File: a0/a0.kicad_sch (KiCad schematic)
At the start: 0 parts

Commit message: update A0
Signed-off-by: Rodney Osodo <socials@rodneyosodo.com>
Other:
- company: (none) -> Abstract Machines
- title: (none) -> A0
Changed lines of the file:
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@@
 	(generator_version "9.0")
 	(paper "A4")
+	(title_block
+		(title "A0")
+		(date "2026-07-03")
+		(rev "v0.4.0")
+		(company "Abstract Machines")
+		(comment 1 "Designed By: Osodo Rodney")
+		(comment 2 "Approved By: Jones Kisaka")
+		(comment 3 "Approved By: Jeff Mboya")
+	)
 	(sheet
 		(at 128.27 78.74)
@@
 		(on_board yes)
 		(dnp no)
-		(fields_autoplaced yes)
 		(stroke
 			(width 0.1524)
@@
 		)
 		(fill
-			(color 0 0 0 0.0000)
+			(color 255 0 0 0.3000)
 		)
 		(property "Sheetname" "power"
-			(at 128.27 78.0284 0)
+			(at 152.654 107.696 0)
 			(effects
 				(font
-					(size 1.27 1.27)
+					(size 7.9756 7.9756)
+					(thickness 1.5951)
+					(bold yes)
 				)
 				(justify left bottom)
@@
 		(on_board yes)
 		(dnp no)
-		(fields_autoplaced yes)
 		(stroke
 			(width 0.1524)
@@
 		)
 		(fill
-			(color 0 0 0 0.0000)
+			(color 255 229 191 1.0000)
 		)
 		(property "Sheetname" "ESP32-C6"
-			(at 31.75 25.9584 0)
+			(at 36.068 50.8 0)
 			(effects
 				(font
-					(size 1.27 1.27)
+					(size 7.9756 7.9756)
+					(thickness 1.5951)
+					(bold yes)
 				)
 				(justify left bottom)
@@
 		(on_board yes)
 		(dnp no)
-		(fields_autoplaced yes)
 		(stroke
 			(width 0.1524)
@@
 		)
 		(fill
-			(color 0 0 0 0.0000)
+			(color 255 255 194 1.0000)
 		)
 		(property "Sheetname" "sim7080G"
-			(at 127 24.6884 0)
+			(at 134.62 50.292 0)
 			(effects
 				(font
-					(size 1.27 1.27)
+					(size 7.9756 7.9756)
+					(thickness 1.5951)
+					(bold yes)
 				)
 				(justify left bottom)
@@
 		(on_board yes)
 		(dnp no)
-		(fields_autoplaced yes)
 		(stroke
 			(width 0.1524)
@@
 		)
 		(fill
-			(color 0 0 0 0.0000)
+			(color 0 0 255 0.3000)
 		)
 		(property "Sheetname" "wmbus"
-			(at 33.02 80.5684 0)
+			(at 47.752 109.474 0)
 			(effects
 				(font
-					(size 1.27 1.27)
+					(size 7.9756 7.9756)
+					(thickness 1.5951)
+					(bold yes)
 				)
 				(justify left bottom)

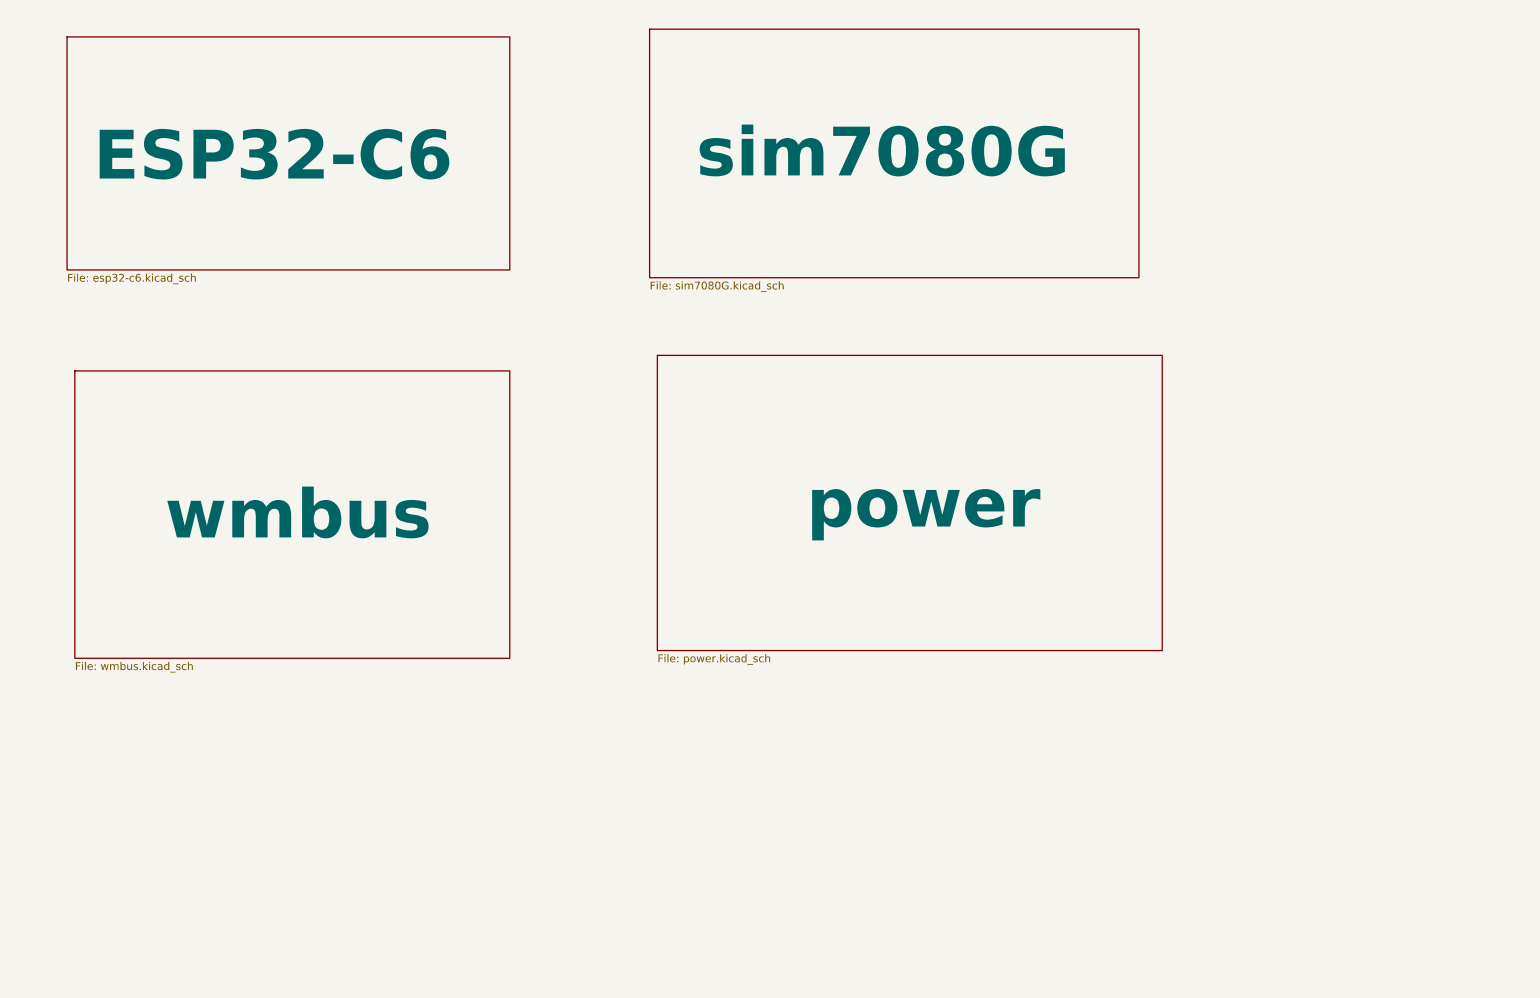
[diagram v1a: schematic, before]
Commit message: fix(A0): update to use modules
Signed-off-by: Rodney Osodo <socials@rodneyosodo.com>
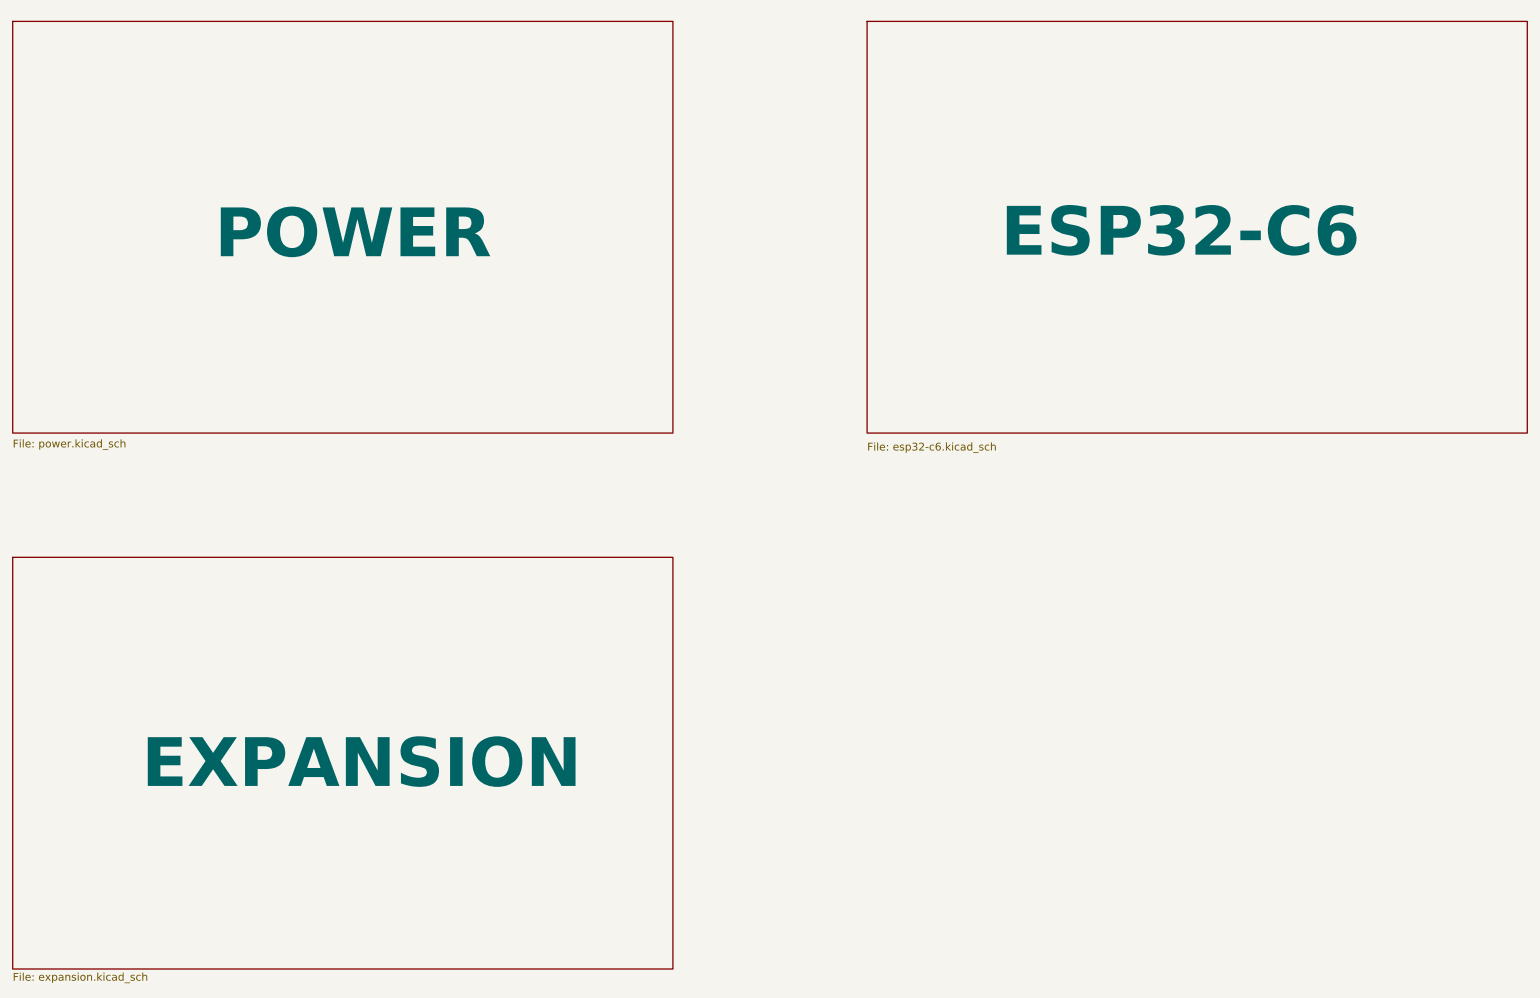
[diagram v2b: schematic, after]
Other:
- sheet power renamed POWER
- removed sheet sim7080G
- removed sheet wmbus
- added sheet EXPANSION (expansion.kicad_sch)
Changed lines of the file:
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@@
 	(title_block
 		(title "A0")
-		(date "2026-07-03")
-		(rev "v0.4.0")
+		(date "2026-07-09")
+		(rev "v0.5.0")
 		(company "Abstract Machines")
 		(comment 1 "Designed By: Osodo Rodney")
@@
 	)
 	(sheet
-		(at 128.27 78.74)
-		(size 82.55 48.26)
+		(at 22.86 24.13)
+		(size 107.95 67.31)
 		(exclude_from_sim no)
 		(in_bom yes)
@@
 			(color 255 0 0 0.3000)
 		)
-		(property "Sheetname" "power"
-			(at 152.654 107.696 0)
+		(property "Sheetname" "POWER"
+			(at 55.88 63.5 0)
 			(effects
 				(font
@@
 		)
 		(property "Sheetfile" "power.kicad_sch"
-			(at 128.27 127.5846 0)
+			(at 22.86 92.456 0)
 			(effects
 				(font
@@
 	)
 	(sheet
-		(at 31.75 26.67)
-		(size 72.39 38.1)
+		(at 22.86 111.76)
+		(size 107.95 67.31)
+		(exclude_from_sim no)
+		(in_bom yes)
+		(on_board yes)
+		(dnp no)
+		(stroke
+			(width 0.1524)
+			(type solid)
+		)
+		(fill
+			(color 132 0 132 0.5000)
+		)
+		(property "Sheetname" "EXPANSION"
+			(at 43.942 150.114 0)
+			(effects
+				(font
+					(size 7.9756 7.9756)
+					(thickness 1.5951)
+					(bold yes)
+				)
+				(justify left bottom)
+			)
+		)
+		(property "Sheetfile" "expansion.kicad_sch"
+			(at 22.86 179.6546 0)
+			(effects
+				(font
+					(size 1.27 1.27)
+				)
+				(justify left top)
+			)
+		)
+		(instances
+			(project "a0"
+				(path "/0ceabfe0-439b-45ca-b804-d1d856d0c97d"
+					(page "4")
+				)
+			)
+		)
+	)
+	(sheet
+		(at 162.56 24.13)
+		(size 107.95 67.31)
 		(exclude_from_sim no)
 		(in_bom yes)
@@
 		)
 		(property "Sheetname" "ESP32-C6"
-			(at 36.068 50.8 0)
+			(at 184.404 63.246 0)
 			(effects
 				(font
@@
 		)
 		(property "Sheetfile" "esp32-c6.kicad_sch"
-			(at 31.75 65.3546 0)
+			(at 162.56 92.964 0)
 			(effects
 				(font
@@
 				)
 			)
-		)
-	)
-	(sheet
-		(at 127 25.4)
-		(size 80.01 40.64)
-		(exclude_from_sim no)
-		(in_bom yes)
-		(on_board yes)
-		(dnp no)
-		(stroke
-			(width 0.1524)
-			(type solid)
-		)
-		(fill
-			(color 255 255 194 1.0000)
-		)
-		(property "Sheetname" "sim7080G"
-			(at 134.62 50.292 0)
-			(effects
-				(font
-					(size 7.9756 7.9756)
-					(thickness 1.5951)
-					(bold yes)
-				)
-				(justify left bottom)
-			)
-		)
-		(property "Sheetfile" "sim7080G.kicad_sch"
-			(at 127 66.6246 0)
-			(effects
-				(font
-					(size 1.27 1.27)
-				)
-				(justify left top)
-			)
-		)
-		(instances
-			(project "a0"
-				(path "/0ceabfe0-439b-45ca-b804-d1d856d0c97d"
-					(page "3")
-				)
-			)
-		)
-	)
-	(sheet
-		(at 33.02 81.28)
-		(size 71.12 46.99)
-		(exclude_from_sim no)
-		(in_bom yes)
-		(on_board yes)
-		(dnp no)
-		(stroke
-			(width 0.1524)
-			(type solid)
-		)
-		(fill
-			(color 0 0 255 0.3000)
-		)
-		(property "Sheetname" "wmbus"
-			(at 47.752 109.474 0)
-			(effects
-				(font
-					(size 7.9756 7.9756)
-					(thickness 1.5951)
-					(bold yes)
-				)
-				(justify left bottom)
-			)
-		)
-		(property "Sheetfile" "wmbus.kicad_sch"
-			(at 33.02 128.8546 0)
-			(effects
-				(font
-					(size 1.27 1.27)
-				)
-				(justify left top)
-			)
-		)
-		(instances
-			(project "a0"
-				(path "/0ceabfe0-439b-45ca-b804-d1d856d0c97d"
-					(page "4")
-				)
-			)
